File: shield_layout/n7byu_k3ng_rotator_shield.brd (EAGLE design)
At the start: 53 x 52.1 mm, 27 parts, among them J1 ARDUINO_R3_SHIELD, J10 ROTCABLE, J2 EL, J3 AZ, J4 ELToggle, J5 I2C-OLD, J6 I2C-NEW, J7 RST, J8 PARK, J9 STOP, Q1 2N3904, Q2 2N3904, Q3 2N3904, Q4 2N3904

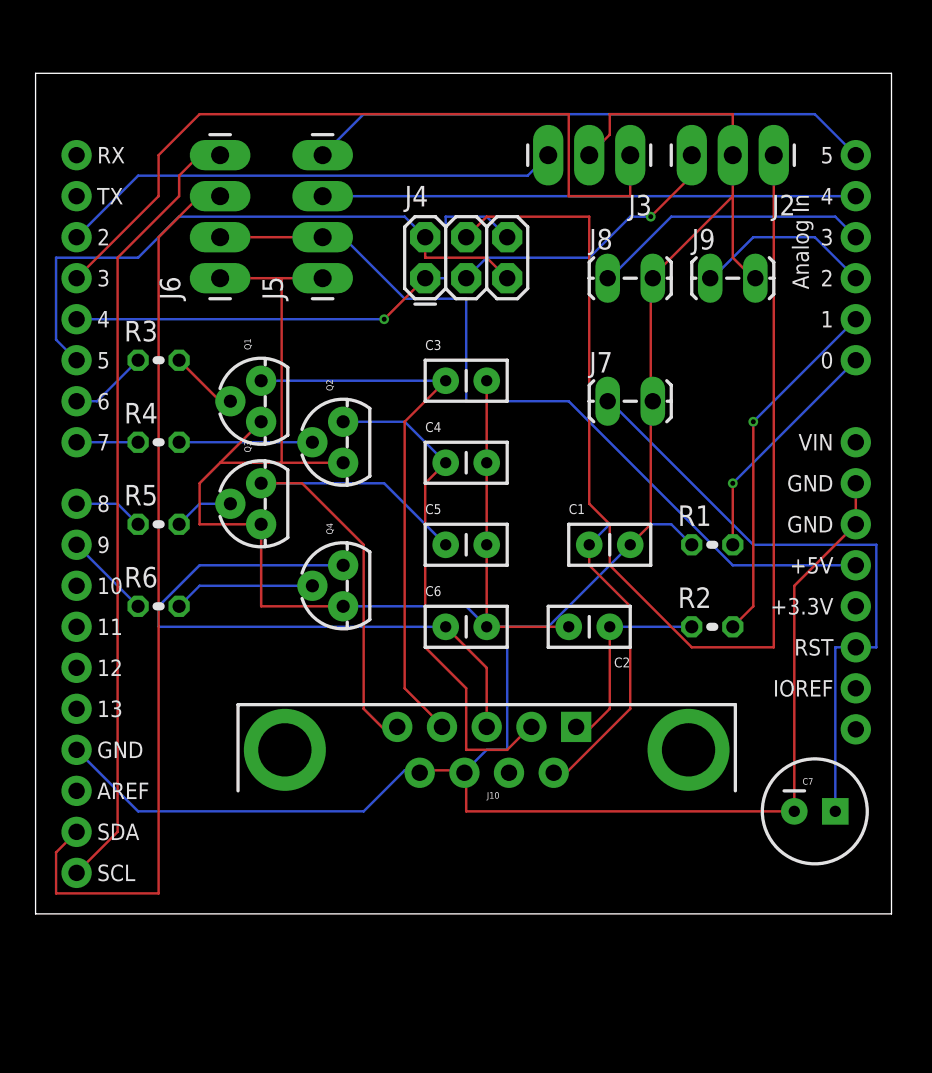
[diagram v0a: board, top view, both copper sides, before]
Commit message: adding pulldown resistors, playing with board
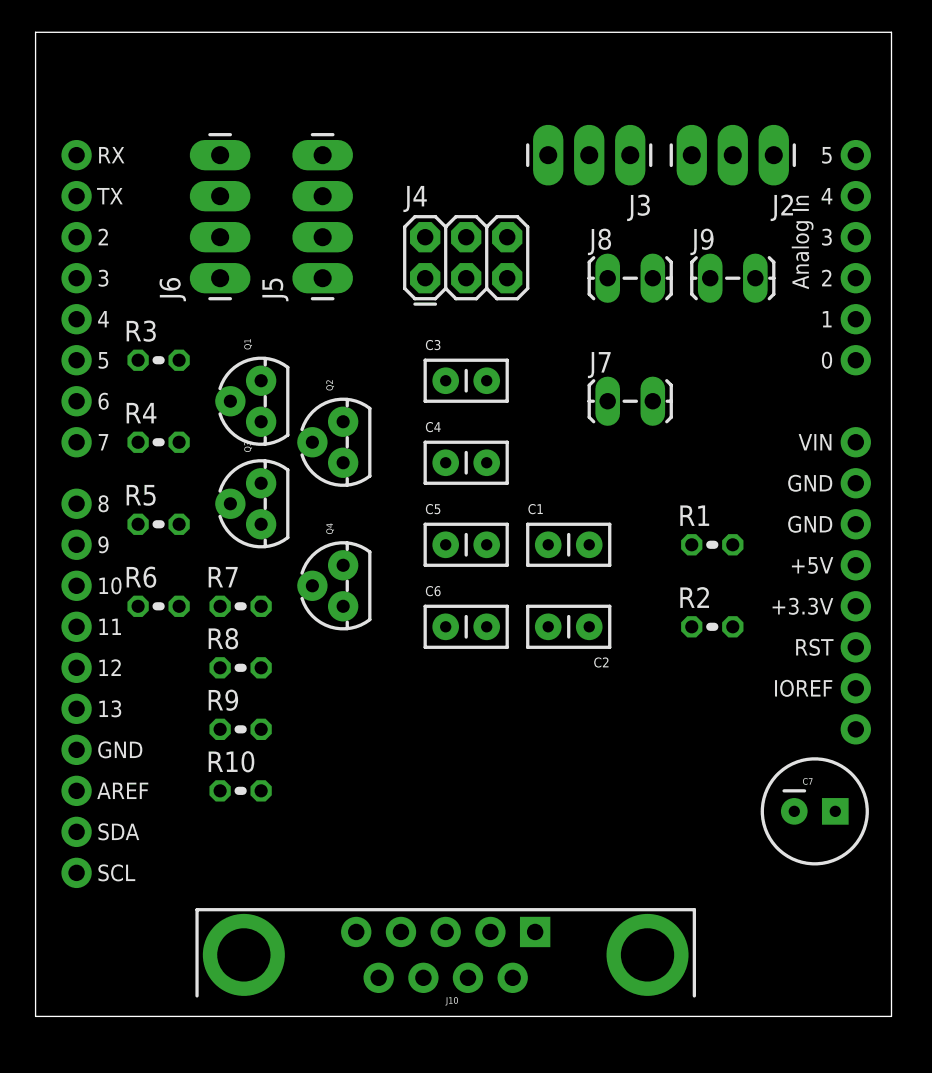
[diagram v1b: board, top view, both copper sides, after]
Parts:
- added R10, R7, R8, R9: 10k, resistor:0204V
- moved J10 13.0 mm to (48.3, 22.9)
- moved C1 2.54 mm to (54.6, 48.3)
- moved C2 1.27 mm to (57.1, 43.2)
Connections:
- net GND: now also R10.1, R7.1, R8.1, R9.1
- net N$2: now also R7.2
- net N$3: now also R8.2
- net N$7: now also R9.2
- net N$8: now also R10.2
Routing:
- net GND: track 216.6 -> 0.00 mm
- net N$14: track 73.0 -> 0.00 mm
- net N$29: track 56.2 -> 0.00 mm
- net N$26: track 51.5 -> 0.00 mm
- net N$32: track 48.9 -> 0.00 mm
- net CCW-BUTTON: track 47.6 -> 0.00 mm
- net N$13: track 39.4 -> 0.00 mm
- net N$12: track 38.9 -> 0.00 mm
- net N$24: track 38.2 -> 0.00 mm
- net N$9: track 35.4 -> 0.00 mm
- net N$25: track 35.1 -> 0.00 mm
- net N$18: track 33.7 -> 0.00 mm
- net N$27: track 33.0 -> 0.00 mm
- net N$23: track 32.1 -> 0.00 mm, vias 1 -> 0
- net N$10: track 31.4 -> 0.00 mm
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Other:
- board size 53 x 52.1 mm -> 53 x 61 mm

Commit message: Adding ARDisable headers and 120ohm Resistor, changing all headers to longpads, and tweaking placement
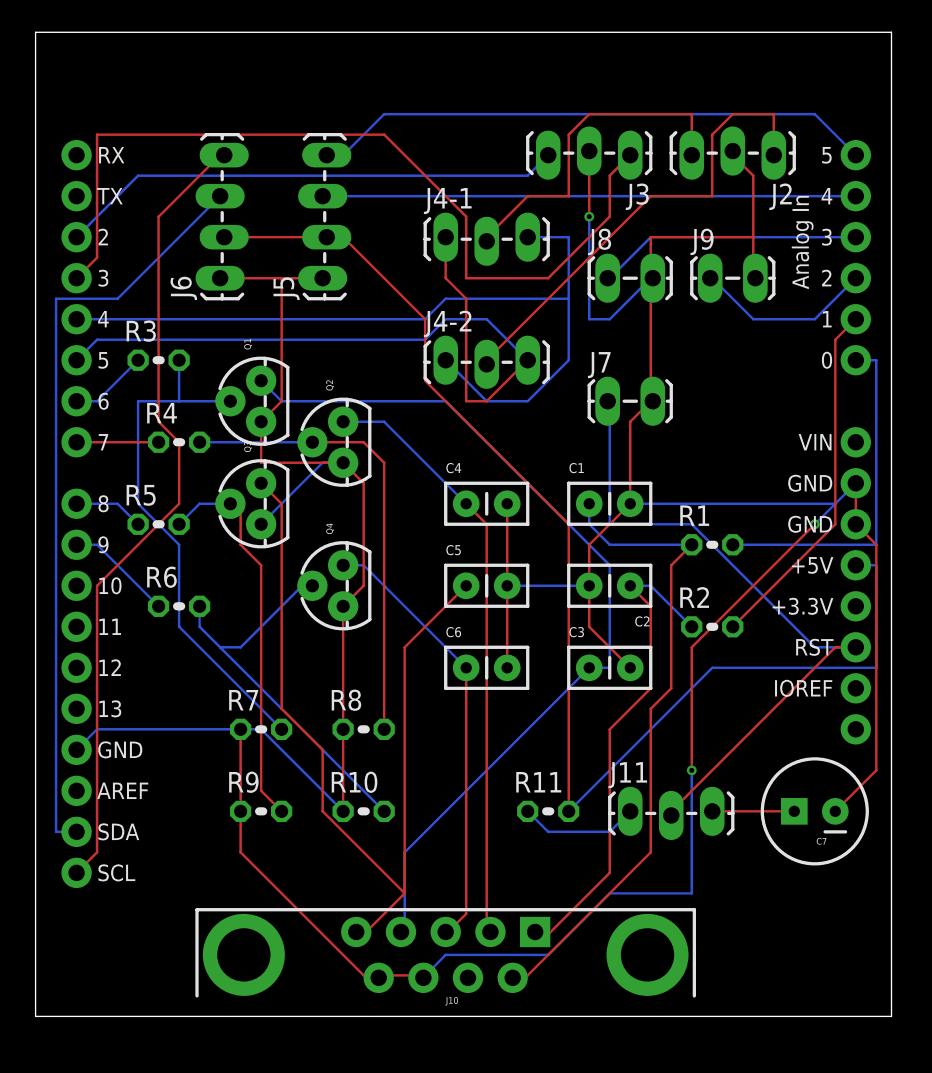
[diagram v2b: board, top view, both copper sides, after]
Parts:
- removed J4: ELToggle, SparkFun-Connectors:2X3
- added J11: ARDisable, SparkFun-Connectors:1X03_LOCK_LONGPADS
- added J4-1, J4-2: ELToggle, SparkFun-Connectors:1X03_LOCK_LONGPADS
- added R11: 120, resistor:0204V
- J2, J3: device SparkFun-Connectors:1X03_LONGPADS -> SparkFun-Connectors:1X03_LOCK_LONGPADS
- J5, J6: device SparkFun-Connectors:1X04_LONGPADS -> SparkFun-Connectors:1X04_LOCK_LONGPADS
- moved C3 19.9 mm to (57.1, 40.6)
- moved R8 8.52 mm to (43.2, 36.8)
- moved R7 7.73 mm to (36.8, 36.8)
- moved R10 7.73 mm to (43.2, 31.8)
- moved R9 5.24 mm to (36.8, 31.8)
- moved C1 3.59 mm to (57.1, 50.8)
- moved C2 3.59 mm to (59.7, 45.7)
- moved C4 2.84 mm to (49.5, 50.8)
- moved C5 2.84 mm to (49.5, 45.7)
- moved C6 2.84 mm to (49.5, 40.6)
- moved R4 1.27 mm to (31.8, 54.6)
- moved R6 1.27 mm to (31.8, 44.5)
- turned C7 to 180 degrees
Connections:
- new net N$11: C7.1, J11.3
- new net N$20: J11.1, R11.1
- net N$13: now also J11.2; no longer C7.1
- net N$14: now also J4-2.2; no longer J4.4
- net N$21: now also J4-1.2; no longer J4.3
- net N$23: now also J4-1.3, J4-2.1; no longer J4.1, J4.6
- net N$24: now also J4-1.1, J4-2.3; no longer J4.2, J4.5
- net N$26: now also R11.2
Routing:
- net GND: track 0.00 -> 252.3 mm, vias 0 -> 3
- net N$26: track 0.00 -> 79.1 mm
- net N$9: track 0.00 -> 55.5 mm
- net N$18: track 0.00 -> 53.8 mm
- net CCW-BUTTON: track 0.00 -> 53.0 mm
- net N$23: track 0.00 -> 50.9 mm
- net N$32: track 0.00 -> 49.4 mm
- net N$29: track 0.00 -> 47.1 mm
- net N$24: track 0.00 -> 45.6 mm
- net N$13: track 0.00 -> 42.0 mm
- net N$1: track 0.00 -> 40.0 mm
- net N$10: track 0.00 -> 37.2 mm
- net N$25: track 0.00 -> 34.9 mm
- net N$27: track 0.00 -> 33.0 mm
- net N$2: track 0.00 -> 32.3 mm
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
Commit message: cleaning up board, renaming components, re-generating Gerber files
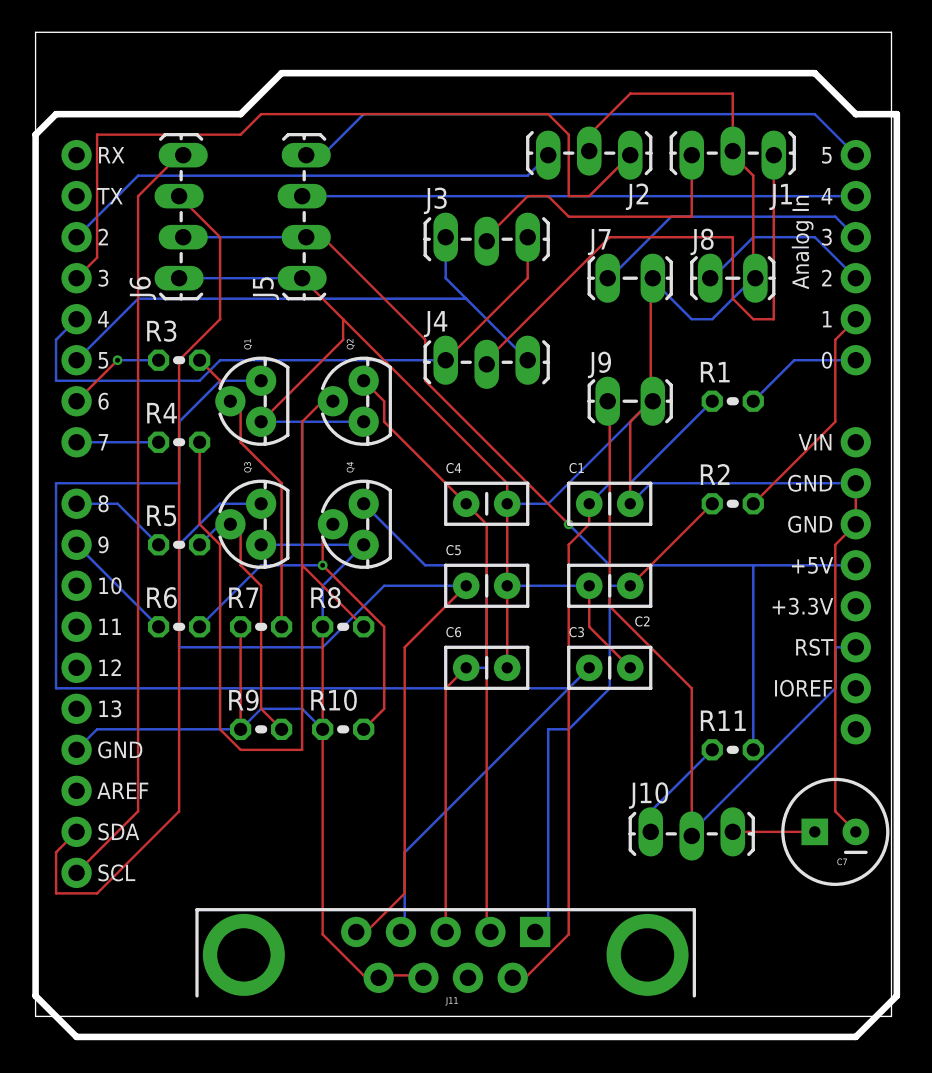
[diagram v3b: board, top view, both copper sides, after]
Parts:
- removed J4-1: ELToggle, SparkFun-Connectors:1X03_LOCK_LONGPADS
- added JARDUINO: ARDUINO_R3_SHIELD, SparkFun-Boards:UNO_R3_SHIELD
- J1: value ARDUINO_R3_SHIELD -> EL; device SparkFun-Boards:UNO_R3_SHIELD -> SparkFun-Connectors:1X03_LOCK_LONGPADS
- J10: value ROTCABLE -> ARDisable; device SparkFun-Connectors:DB9 -> SparkFun-Connectors:1X03_LOCK_LONGPADS
- J11: value ARDisable -> ROTCABLE; device SparkFun-Connectors:1X03_LOCK_LONGPADS -> SparkFun-Connectors:DB9
- J2: value EL -> AZ
- J3: value AZ -> ELToggle
- J7: value RST -> PARK
- J8: value PARK -> STOP
- J9: value STOP -> RST
- moved J1 71.2 mm to (68.6, 72.4), turned to 180 degrees
- moved J10 14.8 mm to (61.0, 30.5), turned to 0 degrees
- moved J11 14.5 mm to (48.3, 22.9), turned to 180 degrees
- moved J3 12.5 mm to (48.3, 67.3), turned to 0 degrees
- moved R11 12.0 mm to (66.0, 35.6)
- moved J9 9.92 mm to (58.4, 57.1)
- moved R1 8.98 mm to (66.0, 57.1)
- moved J2 8.89 mm to (59.7, 72.4)
- moved R2 7.73 mm to (66.0, 50.8)
- moved J7 7.62 mm to (58.4, 64.8)
- moved R8 6.48 mm to (41.9, 43.2)
- moved R7 6.35 mm to (36.8, 43.2)
- moved J8 6.35 mm to (64.8, 64.8)
- moved R10 5.24 mm to (41.9, 36.8)
- moved R9 5.08 mm to (36.8, 36.8)
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- renumbered J4-2 to J4
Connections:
- net CCW-BUTTON: now also J2.1, JARDUINO.D3; no longer J1.D3, J3.1
- net CW-BUTTON: now also J2.3, JARDUINO.D2; no longer J1.D2, J3.3
- net GND: now also J1.2, J11.8, J11.9, JARDUINO.GND@0, JARDUINO.GND@1, JARDUINO.GND@2; no longer J1.GND@0, J1.GND@1, J1.GND@2, J10.8, J10.9, J3.2
- net N$1: now also J11.6; no longer J10.6
- net N$10: now also J11.2; no longer J10.2
- net N$11: now also J10.3; no longer J11.3
- net N$12: now also J11.3; no longer J10.3
- net N$13: now also J10.2, J9.1, JARDUINO.RES; no longer J1.RES, J11.2, J7.1
- net N$14: now also J1.1; no longer J2.1
- net N$15: now also JARDUINO.D6; no longer J1.D6
- net N$16: now also JARDUINO.D7; no longer J1.D7
- net N$17: now also JARDUINO.D8; no longer J1.D8
- net N$18: now also J11.5; no longer J10.5
- net N$19: now also JARDUINO.D9; no longer J1.D9
- net N$20: now also J10.1; no longer J11.1
- net N$21: now also J1.3, J3.2; no longer J2.3, J4-1.2
- net N$22: now also J8.1, JARDUINO.A2; no longer J1.A2, J9.1
- net N$23: now also J3.3, JARDUINO.D4; no longer J1.D4, J4-1.3
- net N$24: now also J3.1, JARDUINO.D5; no longer J1.D5, J4-1.1
- net N$25: now also JARDUINO.A5; no longer J1.A5
- net N$26: now also JARDUINO.5V; no longer J1.5V
- net N$27: now also JARDUINO.A4; no longer J1.A4
- net N$28: now also J7.1, JARDUINO.A3; no longer J1.A3, J8.1
- net N$29: now also JARDUINO.SDA; no longer J1.SDA
- net N$32: now also JARDUINO.SCL; no longer J1.SCL
- net N$4: now also JARDUINO.A0; no longer J1.A0
- net N$5: now also J11.1; no longer J10.1
- net N$6: now also JARDUINO.A1; no longer J1.A1
- net N$9: now also J11.4; no longer J10.4
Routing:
- net N$9: track 55.5 -> 83.5 mm
- net GND: track 252.3 -> 228.3 mm, vias 3 -> 0
- net N$3: track 28.5 -> 52.1 mm
- net N$26: track 79.1 -> 63.0 mm, vias 0 -> 1
- net N$4: track 21.6 -> 7.40 mm
- net N$2: track 32.3 -> 19.4 mm
- net N$23: track 50.9 -> 38.7 mm
- net N$24: track 45.6 -> 35.4 mm
- net N$6: track 22.2 -> 14.1 mm
- net N$7: track 24.4 -> 16.8 mm
- net N$29: track 47.1 -> 54.3 mm
- net N$14: track 29.1 -> 35.7 mm
- net N$12: track 27.4 -> 33.9 mm
- net CCW-BUTTON: track 53.0 -> 48.4 mm
- net N$13: track 42.0 -> 45.8 mm
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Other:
- board size 53 x 61 mm -> 53.3 x 62.2 mm

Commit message: more minor board tweaks, making text easier to read, etc.
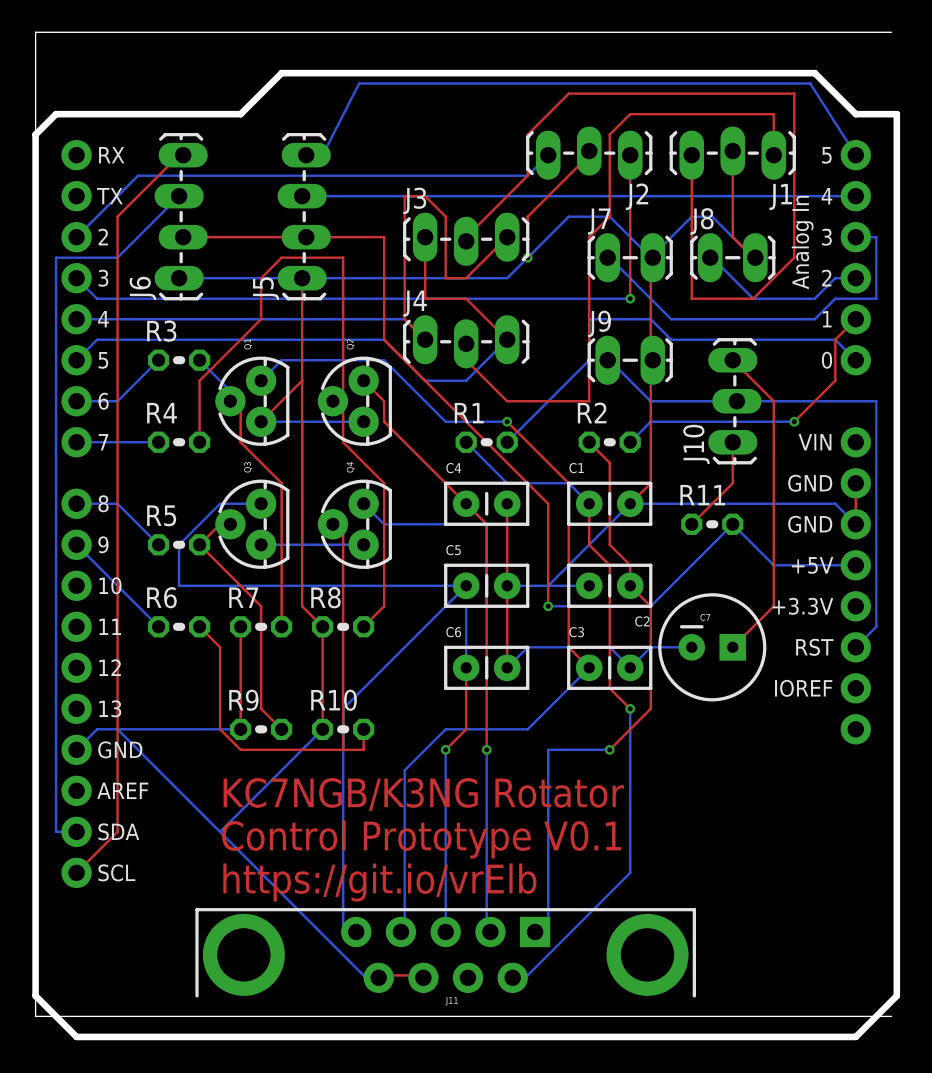
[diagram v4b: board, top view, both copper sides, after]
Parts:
- moved J10 24.7 mm to (66.0, 54.6), turned to 90 degrees
- moved R1 15.5 mm to (50.8, 54.6)
- moved R11 14.0 mm to (64.8, 49.5)
- moved C7 13.7 mm to (64.8, 41.9), turned to 0 degrees
- moved R2 8.52 mm to (58.4, 54.6)
- moved J9 2.54 mm to (58.4, 59.7)
- moved J4 1.80 mm to (47.0, 61.0)
- moved J7 1.27 mm to (58.4, 66.0)
- moved J8 1.27 mm to (64.8, 66.0)
- moved J3 1.27 mm to (47.0, 67.3)
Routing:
- net N$21: track 18.3 -> 52.2 mm
- net N$9: track 83.5 -> 59.2 mm, vias 0 -> 1
- net N$4: track 7.40 -> 27.3 mm
- net N$11: track 5.08 -> 19.9 mm
- net N$13: track 45.8 -> 33.5 mm
- net N$3: track 52.1 -> 42.4 mm
- net N$29: track 54.3 -> 46.0 mm
- net N$8: track 24.6 -> 32.2 mm, vias 1 -> 0
- net N$28: track 17.5 -> 23.8 mm
- net CCW-BUTTON: track 48.4 -> 43.7 mm, vias 0 -> 1
- net N$5: track 33.2 -> 37.7 mm, vias 0 -> 1
- net N$23: track 38.7 -> 43.3 mm
- net N$6: track 14.1 -> 18.6 mm, vias 0 -> 1
- net N$18: track 56.5 -> 52.0 mm
- net N$14: track 35.7 -> 40.0 mm
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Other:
- board text added: "KC7NGB/K3NG Rotator Control Prototype V0.1 https://git.io/vrElb"

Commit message: basic board and schematic cleanup, nothing significant
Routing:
- net GND: track 228.5 -> 225.9 mm
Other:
- board size 53.3 x 62.2 mm -> 53.3 x 59.7 mm
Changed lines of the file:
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@@
 <?xml version="1.0" encoding="utf-8"?>
 <!DOCTYPE eagle SYSTEM "eagle.dtd">
-<eagle version="6.5.0">
+<eagle version="6.6.0">
 <drawing>
 <settings>
@@
 <board>
 <plain>
-<wire x1="22.86" y1="19.05" x2="75.87" y2="19.05" width="0" layer="20"/>
-<wire x1="75.87" y1="80" x2="22.86" y2="80" width="0" layer="20"/>
-<wire x1="22.86" y1="80" x2="22.86" y2="73.66" width="0" layer="20"/>
-<wire x1="22.86" y1="20.32" x2="22.86" y2="19.05" width="0" layer="20"/>
 <wire x1="22.86" y1="73.66" x2="24.13" y2="74.93" width="0.4064" layer="20"/>
 <wire x1="35.56" y1="74.93" x2="24.13" y2="74.93" width="0.4064" layer="20"/>
@@
 <contactref element="C6" pad="2"/>
 <contactref element="JARDUINO" pad="GND@2"/>
-<contactref element="C7" pad="2"/>
 <contactref element="JARDUINO" pad="GND@1"/>
 <contactref element="JARDUINO" pad="GND@0"/>
@@
 <wire x1="67.31" y1="66.04" x2="67.437" y2="66.04" width="0.1524" layer="16"/>
 <wire x1="60.96" y1="41.91" x2="59.69" y2="40.64" width="0.1524" layer="16"/>
-<wire x1="63.5" y1="41.91" x2="60.96" y2="41.91" width="0.1524" layer="16"/>
 <wire x1="73.66" y1="52.07" x2="73.66" y2="49.53" width="0.1524" layer="1"/>
 <wire x1="52.07" y1="45.72" x2="52.07" y2="40.64" width="0.1524" layer="1"/>
@@
 <wire x1="60.96" y1="66.04" x2="61.087" y2="66.04" width="0.1524" layer="16"/>
 <via x="53.34" y="66.04" extent="1-16" drill="0.3048"/>
+<contactref element="C7" pad="2"/>
+<wire x1="60.96" y1="41.91" x2="63.5" y2="41.91" width="0" layer="19" extent="16-16"/>
 </signal>
 <signal name="N$19">
